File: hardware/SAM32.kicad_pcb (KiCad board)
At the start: 4 copper layers, 53.4 x 23.4 mm, 53 parts, among them J1 10118194-0001LF, J2 Conn_01x14, J3 5031821852, J4 B2B-PH-SM4-TB, J5 NPTC072KFMS-RC, J7 Conn_01x17, J96 MOUNTINGHOLE2.5, J97 MOUNTINGHOLE2.5, Q3 DMG341, SW1 KMR231NG LFS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

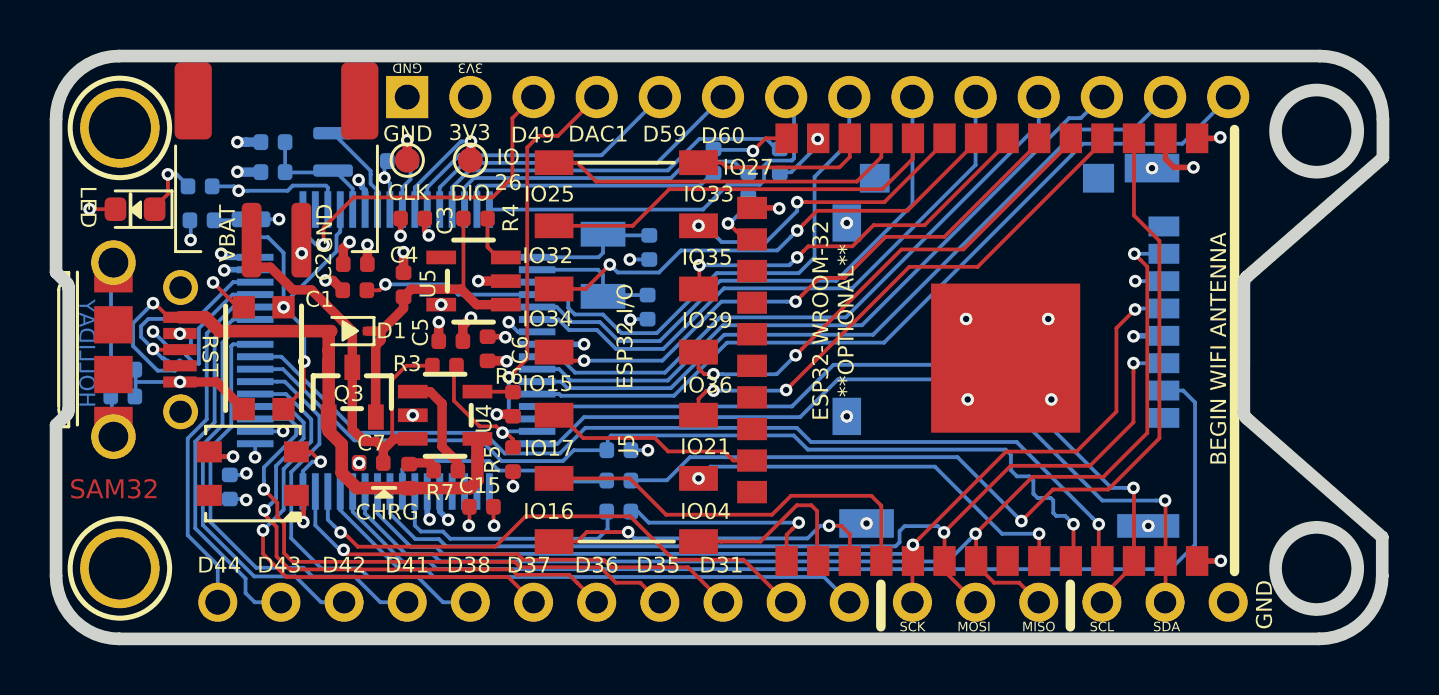
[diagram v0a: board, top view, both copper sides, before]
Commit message: modified board pinout to conform to adafruit feather standard :+1:
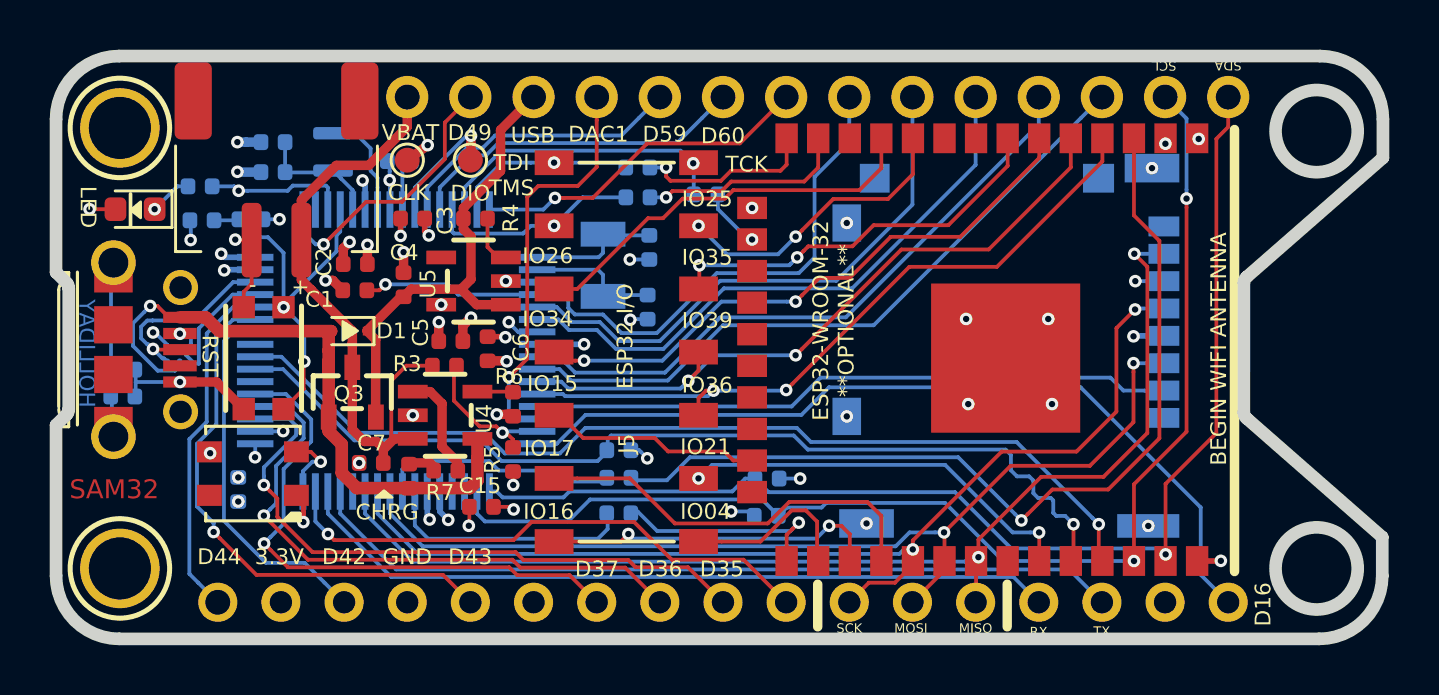
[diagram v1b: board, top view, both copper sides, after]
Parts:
- added R13: 10K, Resistor_SMD:R_0402_1005Metric, B.Cu at (84.4, 106.1)
- added R14: 10K, Resistor_SMD:R_0402_1005Metric, B.Cu at (84.5, 104.6)
- moved R17 5.89 mm to (79.3, 93.3), turned to 0 degrees
- moved R15 3.06 mm to (79.3, 92.1), turned to 0 degrees
- moved R16 1.75 mm to (82.0, 93.2), turned to 0 degrees
- moved C10 0.36 mm to (63.2, 105.0)
- moved R12 0.11 mm to (78.5, 104.6)
- moved R11 0.07 mm to (78.5, 106.0)
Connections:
- C4 pad 1: Net-(C4-Pad1) -> /VIN
- D1 pad 1: Net-(C4-Pad1) -> /VIN
- J2 pad 1: GND -> VBAT
- J2 pad 13: AIN0 -> SCL
- J2 pad 14: AIN1 -> SDA
- J2 pad 2: +3V3 -> D49
- J2 pad 3: D49 -> /VIN
- J4 pad 1: GND -> VBAT
- J4 pad 2: VBAT -> GND
- J5 pad 13: IO33 -> IO25
- J5 pad 14: IO27 -> /TCK
- J5 pad 5: IO32 -> IO26
- J5 pad 6: IO25 -> /TMS
- J5 pad 7: IO26 -> /TDI
- J7 pad 10: D30 -> D31
- J7 pad 11: D29 -> SCK
- J7 pad 12: SCK -> MOSI
- J7 pad 13: MOSI -> MISO
- J7 pad 14: MISO -> RX
- J7 pad 15: SCL -> TX
- J7 pad 16: SDA -> GND
- J7 pad 17: GND -> D16
- J7 pad 2: D43 -> +3V3
- J7 pad 4: D41 -> GND
- J7 pad 5: D38 -> D43
- J7 pad 6: D37 -> Net-(J7-Pad6)
- J7 pad 7: D36 -> D37
- J7 pad 8: D35 -> D36
- J7 pad 9: D31 -> D35
- Q3 pad 2: Net-(C4-Pad1) -> /VIN
- R4 pad 2: Net-(C4-Pad1) -> /VIN
- U2 pad 11: AIN0 -> IO39
- U2 pad 12: AIN1 -> IO36
- U2 pad 13: SCL -> SD_CS
- U2 pad 16: SDA -> D16
- U2 pad 17: AIN2 -> SDA
- U2 pad 18: AIN3 -> SCL
- U2 pad 28: SD_CS -> Net-(U2-Pad28)
- U2 pad 29: D29 -> TX
- U2 pad 30: D30 -> RX
- U5 pad 1: Net-(C4-Pad1) -> /VIN
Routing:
- net D16: track 0.00 -> 33.9 mm
- net TX: track 0.00 -> 33.0 mm
- net AIN1: track 32.8 -> 0.00 mm
- net RX: track 0.00 -> 31.2 mm
- net AIN0: track 30.2 -> 0.00 mm
- net D29: track 22.8 -> 0.00 mm
- net D30: track 22.0 -> 0.00 mm, vias 1 -> 0
- net IO32: track 19.8 -> 0.00 mm, vias 2 -> 0
- net /VIN: track 0.00 -> 19.5 mm
- net D41: track 17.7 -> 0.00 mm
- net SD_CS: track 43.2 -> 25.9 mm
- net SCL: track 31.9 -> 49.2 mm, vias 1 -> 2
- net D38: track 16.8 -> 0.00 mm
- net SDA: track 32.5 -> 48.6 mm
- net Net-(C4-Pad1): track 13.2 -> 0.00 mm
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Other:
- board text added: "+"
- board text added: "-"
- board text added: "3.3V"
- board text added: "D16"
- board text added: "IO26"
- board text added: "RX"
- board text added: "TCK"
- board text added: "TDI"
- board text added: "TMS"
- board text added: "TX"
- board text added: "USB"
- board text removed: "3V3"
- board text removed: "D38"
- board text removed: "D41"
- board text removed: "IO 26"
- board text removed: "IO27"
- board text removed: "IO32"
- board text removed: "IO33"
